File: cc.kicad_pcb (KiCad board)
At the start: 2 copper layers, 78.7 x 73 mm, 44 parts, among them J1 USB_OTG, J2 CONN_PWR, J3 CONN_DEBUG, J4 CONN_USART, J5 CONN_SPI, P1 SMA, SW1 SW_Push, U1 TPS79333, U2 CC1200, U3 BALF-112X-02D3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

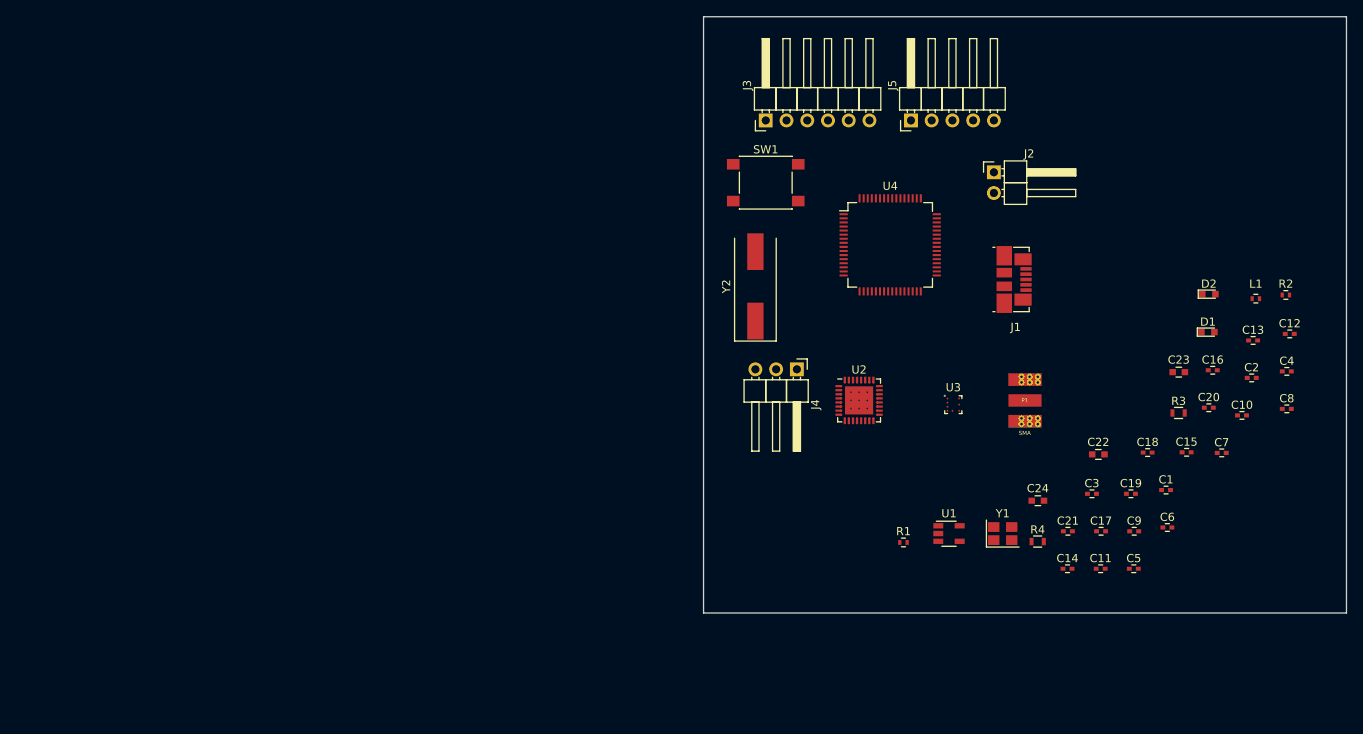
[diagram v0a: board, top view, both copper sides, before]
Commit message: Footprint spreadout
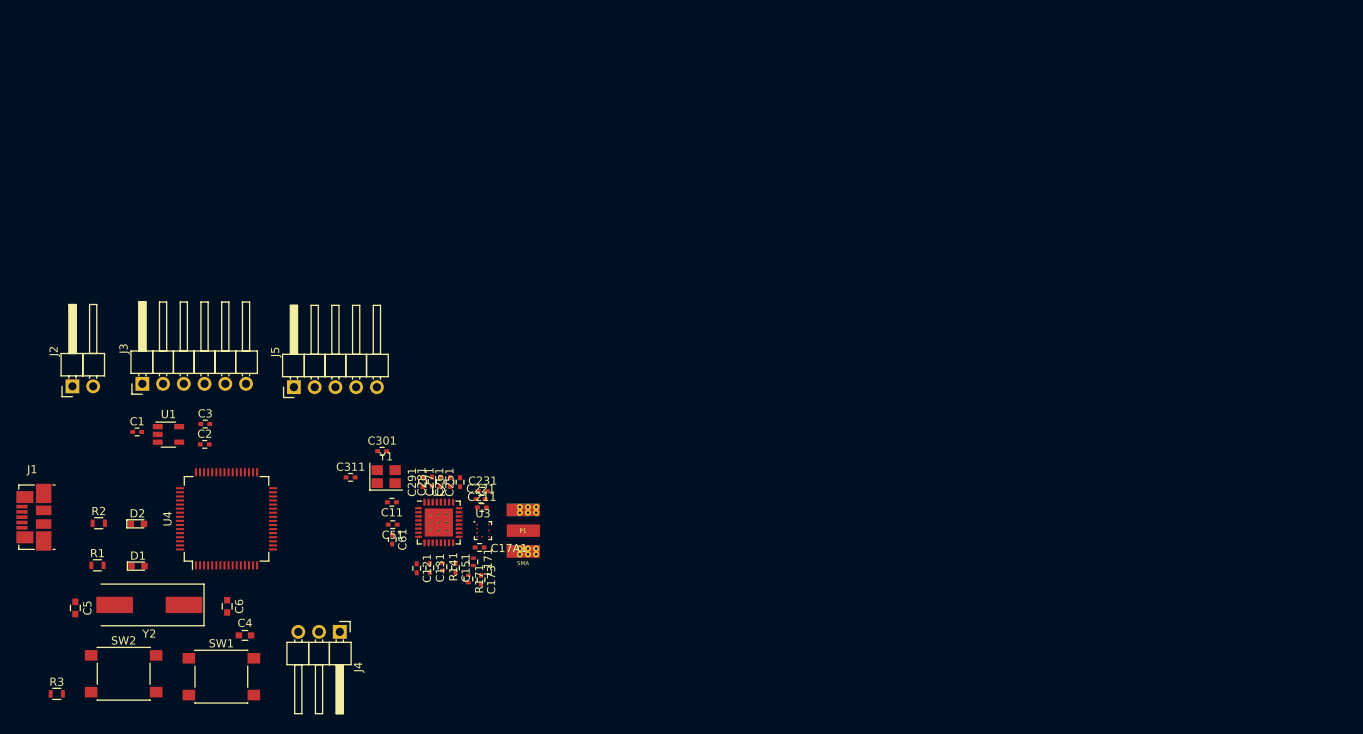
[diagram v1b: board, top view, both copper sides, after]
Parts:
- removed C10, C12, C20, C21, C7, C8, C9: 47nF, Capacitors_SMD:C_0402
- removed C13, C14: 15pF, Capacitors_SMD:C_0402
- removed C15: 1.5nF, Capacitors_SMD:C_0402
- removed C16: 100pF, Capacitors_SMD:C_0402
- removed C17: 56pF, Capacitors_SMD:C_0402
- removed C18: 220nF, Capacitors_SMD:C_0402
- removed C19: 10nF, Capacitors_SMD:C_0402
- removed C22: 104/25V, Capacitors_SMD:C_0603
- removed C23, C24: 200, Capacitors_SMD:C_0603
- removed L1: 56nH, Inductors_SMD:L_0402
- removed R4: 200, Resistors_SMD:R_0603
- added C121: 47nF, Capacitors_SMD:C_0402, F.Cu at (128.7, 119.6)
- added C131: 47nF, Capacitors_SMD:C_0402, F.Cu at (130.3, 119.6)
- added C151: 47nF, Capacitors_SMD:C_0402, F.Cu at (133.5, 119.6)
- added C173: 56pF, Capacitors_SMD:C_0402, F.Cu at (136.6, 121.0)
- added C17A1: 100pF, Capacitors_SMD:C_0402, F.Cu at (136.4, 117.1)
- added C211: 10nF, Capacitors_SMD:C_0402, F.Cu at (136.7, 112.2)
- added C221: 47nF, Capacitors_SMD:C_0402, F.Cu at (136.5, 111.2)
- added C231: 1.5nF, Capacitors_SMD:C_0402, F.Cu at (136.8, 110.2)
- added C251: 47nF, Capacitors_SMD:C_0402, F.Cu at (134.0, 109.1)
- added C261: 47nF, Capacitors_SMD:C_0402, F.Cu at (132.8, 109.1)
- added C271: 47nF, Capacitors_SMD:C_0402, F.Cu at (131.6, 109.0)
- added C281: 47nF, Capacitors_SMD:C_0402, F.Cu at (130.6, 109.0)
- added C291: 47nF, Capacitors_SMD:C_0402, F.Cu at (129.4, 109.1)
- added C301: 15pF, Capacitors_SMD:C_0402, F.Cu at (124.5, 105.3)
- added C311: 15pF, Capacitors_SMD:C_0402, F.Cu at (120.6, 108.5)
- added C51: 47nF, Capacitors_SMD:C_0402, F.Cu at (125.8, 114.3)
- added C61: 220nF, Capacitors_SMD:C_0402, F.Cu at (125.7, 116.1)
- added L171: 56nH, Inductors_SMD:L_0402, F.Cu at (135.6, 118.8)
- added R141: 56k, Resistors_SMD:R_0402, F.Cu at (131.9, 119.4)
- added R171: 18, Resistors_SMD:R_0402, F.Cu at (135.0, 120.9)
- added SW2: SW_Push, Buttons_Switches_SMD:SW_SPST_PTS645, F.Cu at (92.8, 132.5)
- C2: value 2.2uF -> 0.01uF
- C3: value 0.01uF -> 2.2uF
- C4: value 47nF -> 0.1uF/25V; footprint Capacitors_SMD:C_0402 -> Capacitors_SMD:C_0603
- C5, C6: value 47nF -> 20pF; footprint Capacitors_SMD:C_0402 -> Capacitors_SMD:C_0603
- R1: value 18 -> 200; footprint Resistors_SMD:R_0402 -> Resistors_SMD:R_0603
- R2: value 56k -> 200; footprint Resistors_SMD:R_0402 -> Resistors_SMD:R_0603
- R3: value 200 -> 10k
- U4: value STM32F103R8Tx -> STM32L475RC
- moved R2 148.0 mm to (89.8, 114.1)
- moved R3 141.6 mm to (84.6, 135.0)
- moved D2 134.2 mm to (94.5, 114.2)
- moved D1 134.1 mm to (94.6, 119.4)
- moved C4 131.6 mm to (107.7, 127.8)
- moved C5 129.7 mm to (86.9, 124.5), turned to 270 degrees
- moved C2 128.5 mm to (102.7, 104.4)
- moved C1 126.2 mm to (94.5, 102.9)
- moved J1 123.8 mm to (81.7, 113.4), turned to 180 degrees
- moved J2 115.9 mm to (86.5, 97.3), turned to 90 degrees
- moved C6 115.6 mm to (105.5, 124.3), turned to 270 degrees
- moved C3 108.9 mm to (102.8, 102.0)
- moved R1 98.8 mm to (89.6, 119.3)
- moved U1 96.4 mm to (98.3, 103.2)
- moved SW1 90.0 mm to (104.8, 132.9)
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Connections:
- net SWDCLK renamed SWCLK
- C2 pad 1: VDD -> Net-(C2-Pad1)
- C3 pad 1: Net-(C3-Pad1) -> VDD
- C4 pad 1: VDD -> GND
- C4 pad 2: GND -> NRST
- C5 pad 1: VDD -> Net-(C5-Pad1)
- C6 pad 1: VDD -> Net-(C6-Pad1)
- J4 pad 1: USART_TX -> USART_RX
- J4 pad 2: USART_RX -> USART_TX
- J5 pad 1: SPI_NSS -> SPI_MOSI
- J5 pad 2: SPI_SCK -> SPI_MISO
- J5 pad 3: SPI_MISO -> SPI_SCK
- J5 pad 4: SPI_MOSI -> SPI_NSS
- R1 pad 1: Net-(C17-Pad1) -> Net-(D1-Pad1)
- R1 pad 2: VDD -> GND
- R2 pad 1: Net-(R2-Pad1) -> GND
- R2 pad 2: GND -> Net-(D2-Pad1)
- R3 pad 1: Net-(D1-Pad1) -> Net-(R3-Pad1)
- SW1 pad 1: GND -> NRST
- SW1 pad 2: NRST -> GND
- U1 pad 4: Net-(C3-Pad1) -> Net-(C2-Pad1)
- U2 pad 14: Net-(R2-Pad1) -> Net-(R141-Pad1)
- U4 pad 10: (no net) -> Net-(U4-Pad10)
- U4 pad 11: (no net) -> Net-(U4-Pad11)
- U4 pad 12: (no net) -> VSSA
- U4 pad 13: (no net) -> VDDA
- U4 pad 18: VSS -> GND
- U4 pad 2: (no net) -> Net-(U4-Pad2)
- U4 pad 24: (no net) -> Net-(U4-Pad24)
- U4 pad 25: (no net) -> Net-(U4-Pad25)
- U4 pad 26: Net-(D2-Pad2) -> Net-(U4-Pad26)
- U4 pad 27: (no net) -> Net-(U4-Pad27)
- U4 pad 28: (no net) -> Net-(U4-Pad28)
- U4 pad 29: (no net) -> Net-(U4-Pad29)
- U4 pad 3: (no net) -> Net-(U4-Pad3)
- U4 pad 30: (no net) -> Net-(U4-Pad30)
- U4 pad 31: VSS -> GND
- U4 pad 37: (no net) -> Net-(U4-Pad37)
- U4 pad 38: (no net) -> Net-(U4-Pad38)
- U4 pad 39: (no net) -> Net-(U4-Pad39)
- U4 pad 4: (no net) -> Net-(U4-Pad4)
- U4 pad 40: (no net) -> Net-(U4-Pad40)
- U4 pad 47: VSS -> GND
- U4 pad 5: Net-(C23-Pad1) -> Net-(C5-Pad1)
- U4 pad 50: (no net) -> Net-(U4-Pad50)
- U4 pad 51: (no net) -> Net-(U4-Pad51)
- U4 pad 52: (no net) -> Net-(U4-Pad52)
- U4 pad 53: (no net) -> Net-(U4-Pad53)
- U4 pad 54: (no net) -> Net-(U4-Pad54)
- U4 pad 56: (no net) -> Net-(U4-Pad56)
- U4 pad 57: (no net) -> Net-(U4-Pad57)
- U4 pad 58: (no net) -> Net-(U4-Pad58)
- U4 pad 59: (no net) -> Net-(D2-Pad2)
- U4 pad 6: Net-(C24-Pad1) -> Net-(C6-Pad1)
- U4 pad 60: GND -> Net-(R3-Pad1)
- U4 pad 61: (no net) -> Net-(U4-Pad61)
- U4 pad 62: (no net) -> Net-(U4-Pad62)
- U4 pad 63: VSS -> GND
- U4 pad 8: (no net) -> Net-(U4-Pad8)
- U4 pad 9: (no net) -> Net-(U4-Pad9)
- Y2 pad 1: Net-(C24-Pad1) -> Net-(C6-Pad1)
- Y2 pad 2: Net-(C23-Pad1) -> Net-(C5-Pad1)
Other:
- board outline removed
- copper layers 2 -> 4

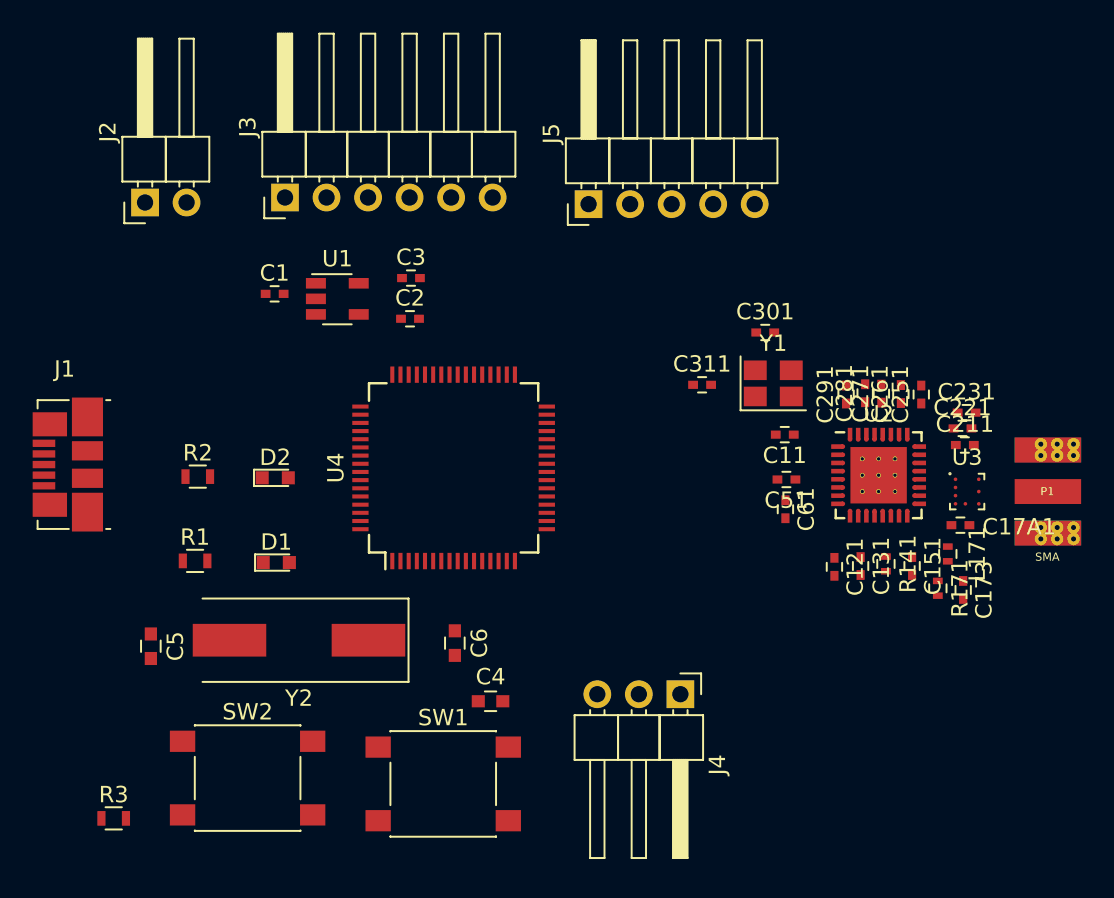
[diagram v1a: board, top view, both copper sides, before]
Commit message: PCB layout WIP
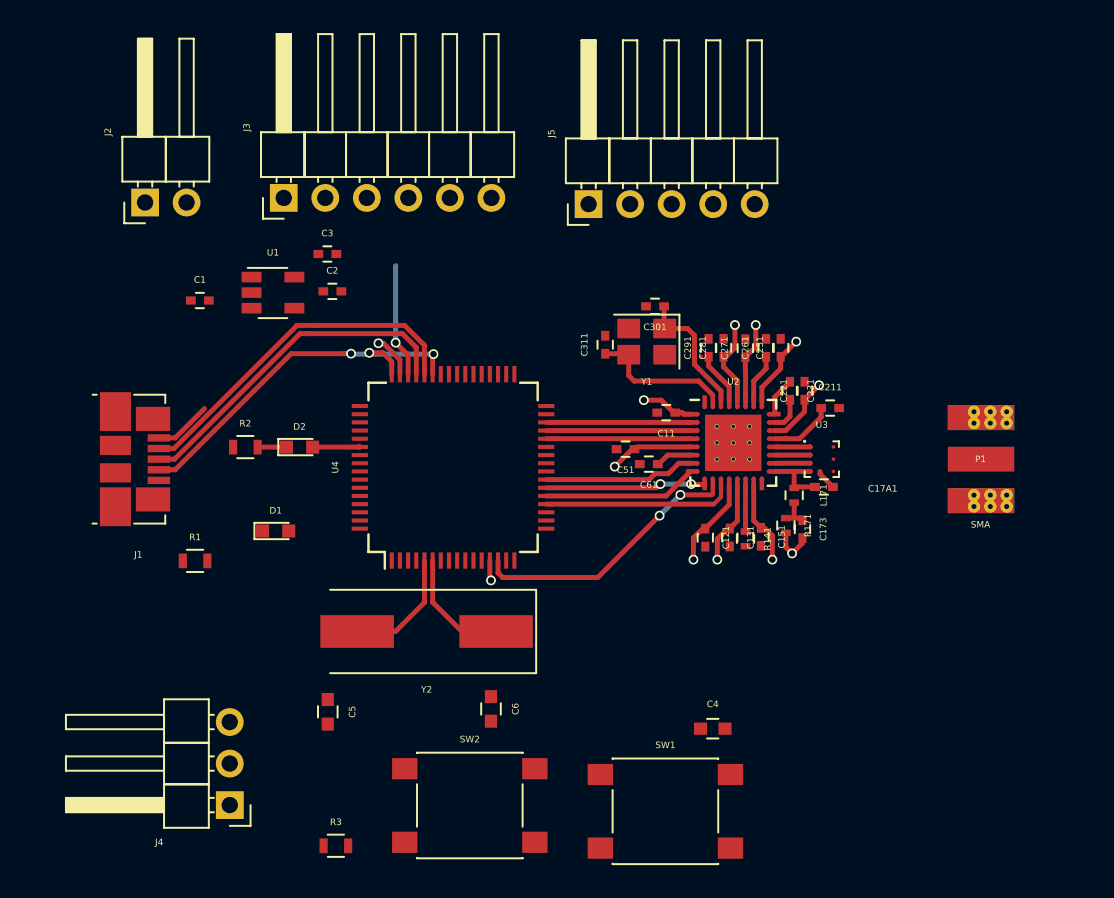
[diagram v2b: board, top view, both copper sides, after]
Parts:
- moved J4 28.4 mm to (91.7, 134.2), turned to 180 degrees
- moved C4 13.7 mm to (121.3, 129.5)
- moved R3 13.7 mm to (98.2, 136.7)
- moved SW1 13.7 mm to (118.4, 134.6)
- moved SW2 13.7 mm to (106.4, 134.2)
- moved C5 11.5 mm to (97.7, 128.5)
- moved C231 10.9 mm to (126.0, 108.8), turned to 270 degrees
- moved C173 10.5 mm to (126.7, 117.3)
- moved L171 10.1 mm to (126.2, 115.2)
- moved R171 10.1 mm to (125.7, 117.1)
- moved C51 10.0 mm to (115.9, 112.4)
- moved C221 9.93 mm to (126.9, 108.8), turned to 90 degrees
- moved C151 9.42 mm to (124.2, 117.8)
- moved U3 9.11 mm to (127.9, 113.0)
- moved U2 9.11 mm to (122.5, 112.0)
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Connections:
- U4 pad 14: CC_GPIO2 -> CC_GPIO0
- U4 pad 15: CC_GPIO3 -> Net-(U4-Pad15)
- U4 pad 16: USART_TX -> Net-(U4-Pad16)
- U4 pad 17: USART_RX -> Net-(U4-Pad17)
- U4 pad 28: Net-(U4-Pad28) -> CC_GPIO2
- U4 pad 29: Net-(U4-Pad29) -> CC_GPIO3
- U4 pad 30: Net-(U4-Pad30) -> CC_RESET_N
- U4 pad 41: CC_GPIO0 -> Net-(U4-Pad41)
- U4 pad 42: CC_RESET_N -> Net-(U4-Pad42)
- U4 pad 54: Net-(U4-Pad54) -> Net-(D2-Pad2)
- U4 pad 58: Net-(U4-Pad58) -> USART_TX
- U4 pad 59: Net-(D2-Pad2) -> USART_RX
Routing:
- net VDD: track 0.00 -> 49.0 mm, vias 0 -> 11
- net USB_DM: track 0.00 -> 21.8 mm
- net USB_DP: track 0.00 -> 21.2 mm
- net USB_ID: track 0.00 -> 21.0 mm, vias 0 -> 2
- net CC_GPIO0: track 0.00 -> 16.7 mm, vias 0 -> 2
- net CC_NSS: track 0.00 -> 11.6 mm
- net CC_MISO: track 0.00 -> 9.79 mm, vias 0 -> 2
- net CC_SCLK: track 0.00 -> 9.51 mm
- net CC_MOSI: track 0.00 -> 9.31 mm
- net Net-(C6-Pad1): track 0.00 -> 9.06 mm
- net CC_RESET_N: track 0.00 -> 8.89 mm
- net CC_GPIO3: track 0.00 -> 8.89 mm
- net CC_GPIO2: track 0.00 -> 8.89 mm
- net Net-(C311-Pad1): track 0.00 -> 8.75 mm
- net Net-(C301-Pad1): track 0.00 -> 8.07 mm
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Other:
- net class Default: clearance 0.2 -> 0.1016
- rule trace_clearance: 0.2 -> 0.1016
- rule trace_min: 0.2 -> 0.127
- rule via_min_drill: 0.3 -> 0.2
- rule via_min_size: 0.4 -> 0.4032

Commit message: Component layout etc.
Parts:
- removed J5: CONN_SPI, Pin_Headers:Pin_Header_Angled_1x05_Pitch2.54mm
- J2: footprint Pin_Headers:Pin_Header_Angled_1x02_Pitch2.54mm -> Pin_Headers:Pin_Header_Straight_1x02_Pitch1.27mm
- J3: footprint Pin_Headers:Pin_Header_Angled_1x06_Pitch2.54mm -> Pin_Headers:Pin_Header_Straight_1x06_Pitch1.27mm
- J4: footprint Pin_Headers:Pin_Header_Angled_1x03_Pitch2.54mm -> Pin_Headers:Pin_Header_Straight_1x03_Pitch1.27mm
- moved R3 24.1 mm to (114.8, 119.3)
- moved SW2 15.3 mm to (117.2, 123.4), turned to 180 degrees
- moved SW1 14.3 mm to (127.4, 123.4)
- moved C4 14.0 mm to (133.2, 122.2), turned to 90 degrees
- moved J4 13.1 mm to (95.0, 121.5)
- moved J3 10.4 mm to (101.6, 105.2)
- moved C1 9.35 mm to (97.8, 108.3)
- moved J2 8.96 mm to (90.9, 105.2)
- moved R1 7.70 mm to (96.2, 115.4), turned to 270 degrees
- moved J1 5.82 mm to (91.9, 113.0)
- moved C3 5.44 mm to (93.9, 104.4), turned to 270 degrees
- moved C6 5.42 mm to (111.4, 124.3)
- moved P1 5.08 mm to (130.6, 113.0)
- moved D1 4.72 mm to (97.0, 113.4)
- moved C5 4.46 mm to (96.2, 124.3)
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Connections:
- U4 pad 10: Net-(U4-Pad10) -> (no net)
- U4 pad 11: Net-(U4-Pad11) -> (no net)
- U4 pad 12: VSSA -> (no net)
- U4 pad 13: VDDA -> (no net)
- U4 pad 15: Net-(U4-Pad15) -> (no net)
- U4 pad 16: Net-(U4-Pad16) -> (no net)
- U4 pad 17: Net-(U4-Pad17) -> (no net)
- U4 pad 2: Net-(U4-Pad2) -> (no net)
- U4 pad 24: Net-(U4-Pad24) -> (no net)
- U4 pad 25: Net-(U4-Pad25) -> (no net)
- U4 pad 26: Net-(U4-Pad26) -> (no net)
- U4 pad 27: Net-(U4-Pad27) -> (no net)
- U4 pad 3: Net-(U4-Pad3) -> (no net)
- U4 pad 33: SPI_NSS -> (no net)
- U4 pad 34: SPI_SCK -> (no net)
- U4 pad 35: SPI_MISO -> (no net)
- U4 pad 36: SPI_MOSI -> (no net)
- U4 pad 37: Net-(U4-Pad37) -> (no net)
- U4 pad 38: Net-(U4-Pad38) -> (no net)
- U4 pad 39: Net-(U4-Pad39) -> (no net)
- U4 pad 4: Net-(U4-Pad4) -> (no net)
- U4 pad 40: Net-(U4-Pad40) -> (no net)
- U4 pad 41: Net-(U4-Pad41) -> (no net)
- U4 pad 42: Net-(U4-Pad42) -> (no net)
- U4 pad 50: Net-(U4-Pad50) -> (no net)
- U4 pad 51: Net-(U4-Pad51) -> (no net)
- U4 pad 52: Net-(U4-Pad52) -> (no net)
- U4 pad 53: Net-(U4-Pad53) -> (no net)
- U4 pad 56: Net-(U4-Pad56) -> (no net)
- U4 pad 57: Net-(U4-Pad57) -> (no net)
- U4 pad 61: Net-(U4-Pad61) -> (no net)
- U4 pad 62: Net-(U4-Pad62) -> (no net)
- U4 pad 8: Net-(U4-Pad8) -> (no net)
- U4 pad 9: Net-(U4-Pad9) -> (no net)
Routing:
- net NRST: track 0.00 -> 47.2 mm, vias 0 -> 4
- net GND: track 2.95 -> 32.0 mm, vias 1 -> 3
- net Net-(R3-Pad1): track 0.00 -> 26.5 mm, vias 0 -> 2
- net +5V: track 3.53 -> 17.0 mm
- net SWCLK: track 0.00 -> 10.1 mm, vias 0 -> 2
- net USB_DM: track 21.8 -> 12.8 mm, vias 0 -> 2
- net USART_RX: track 0.00 -> 8.95 mm
- net USB_DP: track 21.2 -> 12.5 mm, vias 0 -> 2
- net USART_TX: track 0.00 -> 8.37 mm
- net USB_ID: track 21.0 -> 14.9 mm
- net VDD: track 49.0 -> 52.8 mm, vias 11 -> 14
- net Net-(P1-Pad1): track 0.00 -> 3.67 mm
- net Net-(C6-Pad1): track 9.06 -> 12.4 mm
- net Net-(C5-Pad1): track 7.42 -> 10.8 mm
- net SWDIO: track 6.98 -> 4.89 mm, vias 1 -> 0
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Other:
- board outline added: 45.7 x 23.7 mm
- net class Default: trace_width 0.25 -> 0.305

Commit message: Polishing
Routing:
- net GND: track 32.0 -> 59.1 mm, vias 3 -> 10
- net VDD: track 52.8 -> 62.3 mm, vias 14 -> 18
- net Net-(C301-Pad1): track 8.43 -> 7.84 mm
- net Net-(C311-Pad1): track 8.20 -> 7.67 mm
- added copper zone on B.Cu, net GND
- added copper zone on F.Cu, net GND
- added copper zone on In1.Cu, net GND
- added copper zone on In2.Cu, net VDD
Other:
- board text added: "CC1200 Module By Shih En 2017/3/20"

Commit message: Layout
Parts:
- added GND: GND, gsg-modules:TESTPOINT-50MIL, F.Cu at (90.7, 125.3)
- moved Y1 0.18 mm to (117.1, 106.8)
- moved C311 0.18 mm to (114.6, 106.8)
- moved C301 0.17 mm to (117.1, 104.6)
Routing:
- net GND: track 59.1 -> 88.2 mm, vias 10 -> 14
- net SWO: track 0.00 -> 11.9 mm, vias 0 -> 2
- net VDD: track 62.3 -> 62.9 mm
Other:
- board text added: "CC1200 Module rev 0.1.0 By Shih En 2017/3/20"
- board text removed: "CC1200 Module By Shih En 2017/3/20"

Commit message: Pre v0.1.0
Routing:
- net GND: track 88.2 -> 87.3 mm
